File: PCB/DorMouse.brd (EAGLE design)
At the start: 63.3 x 90.1 mm, 55 parts, among them IC1 LM340MP-05, IC2 MAX1551, U1 STM32F10XRXT6, X1 MINI-USB-UX60-MB-5ST

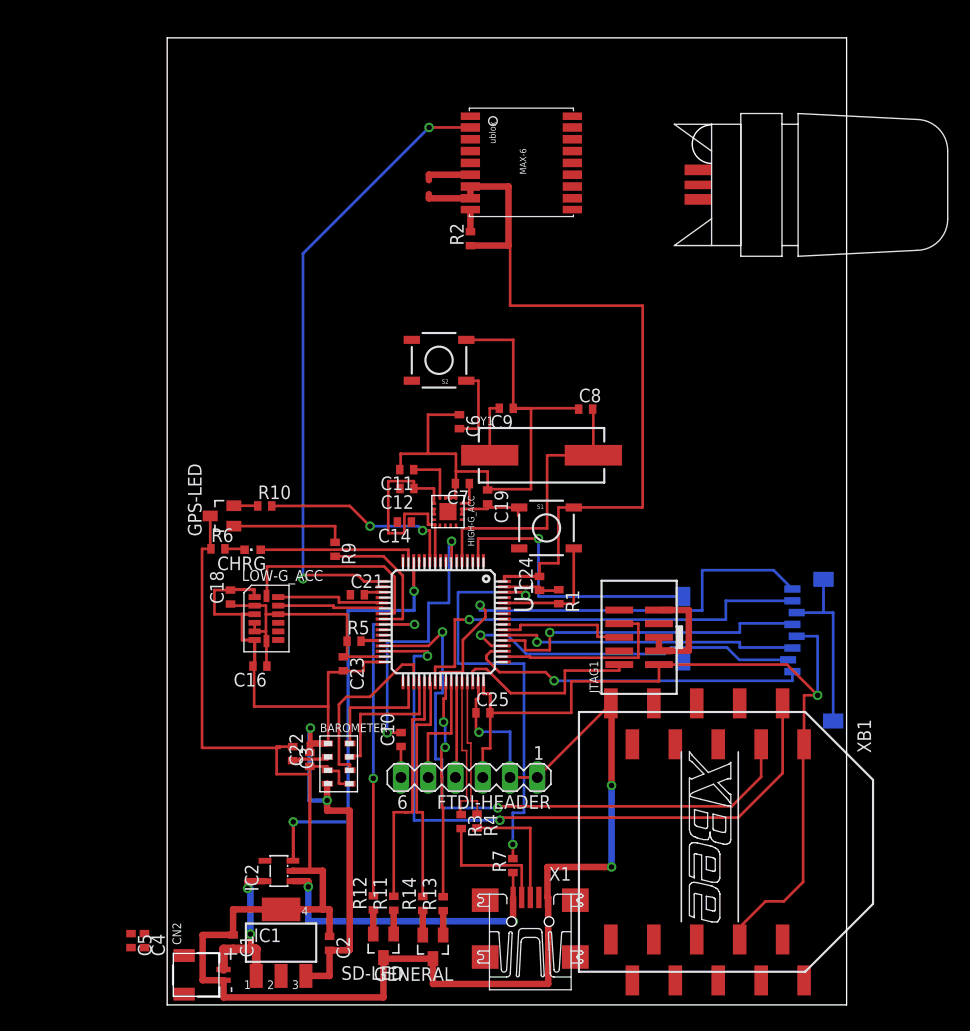
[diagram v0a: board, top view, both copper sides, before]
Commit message: Sync older board with schematic
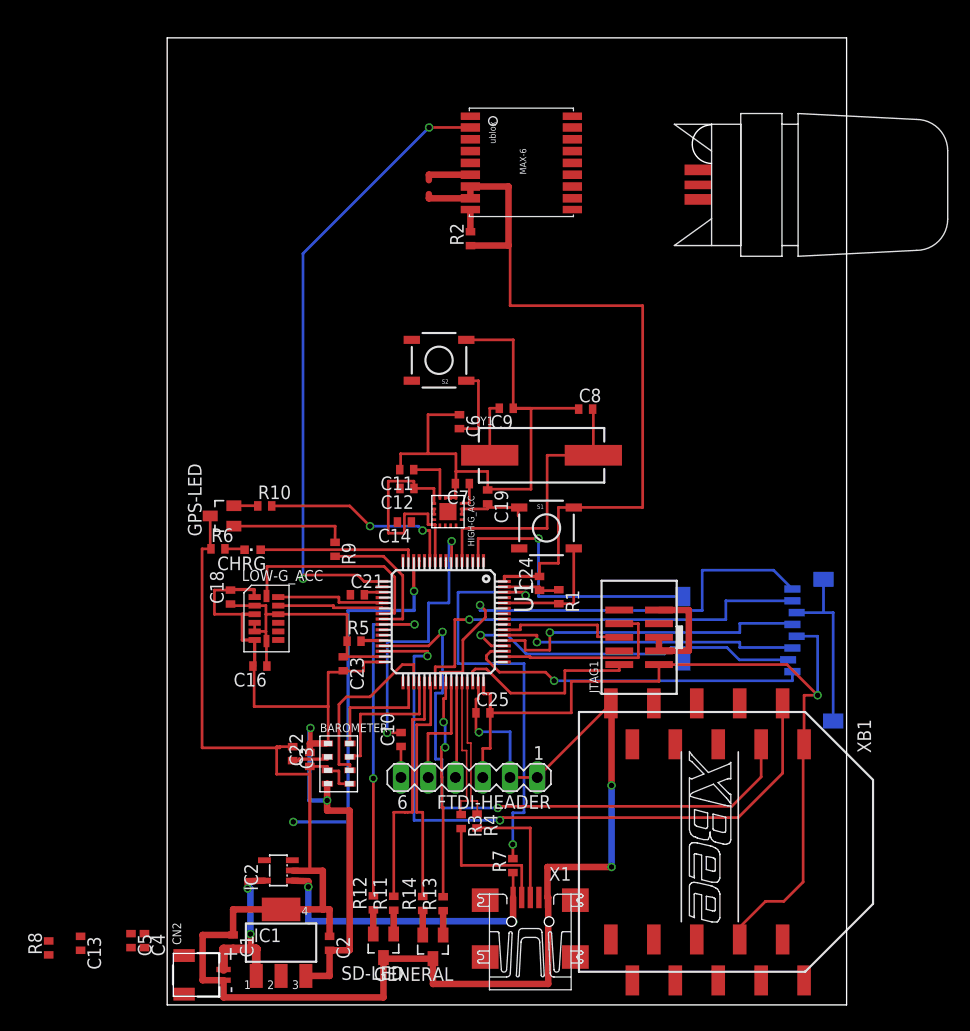
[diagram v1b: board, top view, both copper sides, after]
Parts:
- added C13: 1uF, rcl:C0402
- added R8: 100k, rcl:R0402
- moved IC2 0.07 mm to (10.4, 12.5)
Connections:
- new net N$13: IC2.3, R8.1
- net CHARGING(-): now also R8.2; no longer IC2.3
- net GND: now also C13.1
- net USB-5V: now also C13.2
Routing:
- net CHARGING(-): track 39.3 -> 35.6 mm
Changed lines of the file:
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@@
 </class>
 </classes>
-<designrules name="default">
+<designrules name="Fusion_eagle_rule_v1.1">
 <description language="de">&lt;b&gt;EAGLE Design Rules&lt;/b&gt;
 &lt;p&gt;
@@
 necessary adjustments and save your customized
 design rules under a new name.</description>
+<description language="zh">&lt;b&gt;Seeed Studio EAGLE Design Rules&lt;/b&gt;
+</description>
 <param name="layerSetup" value="(1*16)"/>
 <param name="mtCopper" value="0.035mm 0.035mm 0.035mm 0.035mm 0.035mm 0.035mm 0.035mm 0.035mm 0.035mm 0.035mm 0.035mm 0.035mm 0.035mm 0.035mm 0.035mm 0.035mm"/>
 <param name="mtIsolate" value="1.5mm 0.15mm 0.2mm 0.15mm 0.2mm 0.15mm 0.2mm 0.15mm 0.2mm 0.15mm 0.2mm 0.15mm 0.2mm 0.15mm 0.2mm"/>
-<param name="mdWireWire" value="8mil"/>
-<param name="mdWirePad" value="8mil"/>
-<param name="mdWireVia" value="8mil"/>
-<param name="mdPadPad" value="8mil"/>
-<param name="mdPadVia" value="8mil"/>
-<param name="mdViaVia" value="8mil"/>
-<param name="mdSmdPad" value="8mil"/>
-<param name="mdSmdVia" value="8mil"/>
-<param name="mdSmdSmd" value="8mil"/>
+<param name="mdWireWire" value="6mil"/>
+<param name="mdWirePad" value="6mil"/>
+<param name="mdWireVia" value="6mil"/>
+<param name="mdPadPad" value="6mil"/>
+<param name="mdPadVia" value="6mil"/>
+<param name="mdViaVia" value="6mil"/>
+<param name="mdSmdPad" value="0mil"/>
+<param name="mdSmdVia" value="0mil"/>
+<param name="mdSmdSmd" value="0mil"/>
 <param name="mdViaViaSameLayer" value="8mil"/>
 <param name="mnLayersViaInSmd" value="2"/>
-<param name="mdCopperDimension" value="40mil"/>
-<param name="mdDrill" value="8mil"/>
+<param name="mdCopperDimension" value="10mil"/>
+<param name="mdDrill" value="10mil"/>
 <param name="mdSmdStop" value="0mil"/>
-<param name="msWidth" value="10mil"/>
-<param name="msDrill" value="24mil"/>
-<param name="msMicroVia" value="9.99mm"/>
+<param name="msWidth" value="6mil"/>
+<param name="msDrill" value="12mil"/>
+<param name="msMicroVia" value="12mil"/>
 <param name="msBlindViaRatio" value="0.5"/>
 <param name="rvPadTop" value="0.25"/>
@@
 <param name="rlMinPadBottom" value="10mil"/>
 <param name="rlMaxPadBottom" value="20mil"/>
-<param name="rlMinViaOuter" value="8mil"/>
+<param name="rlMinViaOuter" value="6mil"/>
 <param name="rlMaxViaOuter" value="20mil"/>
-<param name="rlMinViaInner" value="8mil"/>
+<param name="rlMinViaInner" value="6mil"/>
 <param name="rlMaxViaInner" value="20mil"/>
 <param name="rlMinMicroViaOuter" value="4mil"/>
@@
 <param name="psTop" value="-1"/>
 <param name="psBottom" value="-1"/>
-<param name="psFirst" value="-1"/>
+<param name="psFirst" value="0"/>
 <param name="psElongationLong" value="100"/>
 <param name="psElongationOffset" value="100"/>
 <param name="mvStopFrame" value="1"/>
 <param name="mvCreamFrame" value="0"/>
-<param name="mlMinStopFrame" value="4mil"/>
-<param name="mlMaxStopFrame" value="4mil"/>
+<param name="mlMinStopFrame" value="2mil"/>
+<param name="mlMaxStopFrame" value="2mil"/>
 <param name="mlMinCreamFrame" value="0mil"/>
 <param name="mlMaxCreamFrame" value="0mil"/>
-<param name="mlViaStopLimit" value="0mil"/>
+<param name="mlViaStopLimit" value="100mil"/>
 <param name="srRoundness" value="0"/>
 <param name="srMinRoundness" value="0mil"/>
@@
 <param name="checkAngle" value="0"/>
 <param name="checkFont" value="1"/>
-<param name="checkRestrict" value="1"/>
+<param name="checkRestrict" value="0"/>
 <param name="useDiameter" value="13"/>
 <param name="maxErrors" value="50"/>
@@
 <element name="C1" library="rcl" package="C0402" value="0.22uF" x="6.14" y="5.87" rot="R270"/>
 <element name="C2" library="rcl" package="C0402" value="0.1uF" x="15.13" y="5.74" rot="R270"/>
-<element name="IC2" library="maxim" package="SOT23-5L" value="MAX1551" x="10.41" y="12.48" rot="R90">
-<attribute name="OC_NEWARK" value="88H0599" x="70.1" y="83.6" size="1.778" layer="27" rot="R90" display="off"/>
-<attribute name="MPN" value="MAX1551EZK-T" x="70.1" y="83.6" size="1.778" layer="27" rot="R90" display="off"/>
-<attribute name="MF" value="MAXIM" x="70.1" y="83.6" size="1.778" layer="27" rot="R90" display="off"/>
-<attribute name="OC_FARNELL" value="1628221" x="70.1" y="83.6" size="1.778" layer="27" rot="R90" display="off"/>
+<element name="IC2" library="maxim" package="SOT23-5L" value="MAX1551" x="10.36" y="12.53" rot="R90">
+<attribute name="OC_NEWARK" value="88H0599" x="70.05" y="83.65" size="1.778" layer="27" rot="R90" display="off"/>
+<attribute name="MPN" value="MAX1551EZK-T" x="70.05" y="83.65" size="1.778" layer="27" rot="R90" display="off"/>
+<attribute name="MF" value="MAXIM" x="70.05" y="83.65" size="1.778" layer="27" rot="R90" display="off"/>
+<attribute name="OC_FARNELL" value="1628221" x="70.05" y="83.65" size="1.778" layer="27" rot="R90" display="off"/>
 </element>
 <element name="X1" library="con-hirose" package="UX60-MB-5ST" value="MINI-USB-UX60-MB-5ST" x="33.83" y="7.76" rot="R90">
@@
 <element name="C5" library="rcl" package="C0402" value="4.7uF" x="-3.37" y="5.99" rot="R270"/>
 <element name="U$1" library="Ava" package="SARANTEL-SR1202" value="SARANTEL-SR1202" x="49.45" y="76.4"/>
+<element name="C13" library="rcl" package="C0402" value="1uF" x="-8.07" y="5.74" rot="R270"/>
+<element name="R8" library="rcl" package="R0402" value="100k" x="-11.04" y="5.31" rot="R90"/>
 </elements>
 <signals>
@@
 <wire x1="15.13" y1="8.899" x2="14.5" y2="8.899" width="0.6096" layer="1"/>
 <wire x1="14.5" y1="8.899" x2="10.61" y2="8.899" width="0.6096" layer="1"/>
-<wire x1="11.71" y1="12.48" x2="11.71" y2="12.5" width="0.6096" layer="1"/>
+<wire x1="11.66" y1="12.53" x2="11.71" y2="12.5" width="0" layer="19" extent="1-16"/>
 <wire x1="11.71" y1="12.5" x2="14.5" y2="12.5" width="0.6096" layer="1"/>
 <wire x1="14.5" y1="12.5" x2="14.5" y2="8.899" width="0.6096" layer="1"/>
@@
 <contactref element="U1" pad="12"/>
 <wire x1="23.97" y1="41.4" x2="24" y2="41.4" width="0.254" layer="1"/>
+<contactref element="C13" pad="1"/>
 <wire x1="49.45" y1="75.05" x2="49.45" y2="77.8" width="0" layer="19" extent="1-1"/>
 <wire x1="37.75" y1="74.1" x2="49.45" y2="75.05" width="0" layer="19" extent="1-1"/>
@@
 <wire x1="-2.12" y1="5.34" x2="3.3" y2="6.52" width="0" layer="19" extent="1-1"/>
 <wire x1="-3.37" y1="6.64" x2="-2.12" y2="5.34" width="0" layer="19" extent="1-1"/>
+<wire x1="-8.07" y1="6.39" x2="-3.37" y2="6.64" width="0" layer="19" extent="1-1"/>
 <wire x1="45.82" y1="33" x2="41.4" y2="28.098" width="0" layer="19" extent="1-1"/>
 <wire x1="48.05" y1="32.05" x2="48.6" y2="33" width="0" layer="19" extent="1-16"/>
@@
 <wire x1="8.2986" y1="5.22" x2="8.2986" y2="5.2" width="0.8128" layer="1"/>
 <wire x1="8.2986" y1="5.2" x2="7.4" y2="5.2" width="0.8128" layer="1"/>
-<wire x1="9.11" y1="11.53" x2="7.5" y2="11.53" width="0.6096" layer="1"/>
+<wire x1="9.06" y1="11.58" x2="7.5" y2="11.53" width="0.6096" layer="1"/>
 <wire x1="7.5" y1="11.53" x2="7.5" y2="10.85" width="0.6096" layer="1"/>
 <via x="7.5" y="10.85" extent="1-16" drill="0.5" shape="octagon"/>
@@
 <contactref element="X1" pad="1"/>
 <contactref element="R7" pad="1"/>
-<wire x1="11.71" y1="11.53" x2="13.15" y2="11.53" width="0.6096" layer="1"/>
+<wire x1="11.66" y1="11.58" x2="13.15" y2="11.53" width="0.6096" layer="1"/>
 <wire x1="13.15" y1="11.53" x2="13.15" y2="11" width="0.6096" layer="1"/>
 <via x="13.15" y="11" extent="1-16" drill="0.5" shape="octagon"/>
@@
 <wire x1="32.23" y1="10.01" x2="32.23" y2="12.33" width="0.254" layer="1"/>
 <wire x1="32.23" y1="12.33" x2="32.21" y2="12.33" width="0.254" layer="1"/>
+<contactref element="C13" pad="2"/>
+<wire x1="-8.07" y1="5.09" x2="11.66" y2="11.58" width="0" layer="19" extent="1-1"/>
 </signal>
 <signal name="CHARGING(-)">
-<contactref element="IC2" pad="3"/>
 <contactref element="U1" pad="14"/>
-<wire x1="11.71" y1="13.43" x2="11.75" y2="13.43" width="0.3048" layer="1"/>
-<wire x1="11.75" y1="13.43" x2="11.75" y2="17.05" width="0.3048" layer="1"/>
 <via x="11.75" y="17.05" extent="1-16" drill="0.5" shape="octagon"/>
 <wire x1="11.75" y1="17.05" x2="16.85" y2="17.05" width="0.3048" layer="16"/>
@@
 <wire x1="23" y1="38.55" x2="22.97" y2="38.55" width="0.3048" layer="1"/>
 <wire x1="22.97" y1="38.55" x2="22.97" y2="41.4" width="0.3048" layer="1"/>
+<contactref element="R8" pad="2"/>
+<wire x1="-11.04" y1="5.96" x2="22.97" y2="41.4" width="0" layer="19" extent="1-16"/>
 </signal>
 <signal name="MOSI-1">
@@
 <wire x1="33.4" y1="38.45" x2="31.42" y2="38.45" width="0.254" layer="1"/>
 </signal>
+<signal name="N$13">
+<contactref element="R8" pad="1"/>
+<contactref element="IC2" pad="3"/>
+<wire x1="11.66" y1="13.48" x2="-11.04" y2="4.66" width="0" layer="19" extent="1-16"/>
+</signal>
 </signals>

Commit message: Most of the pcb done
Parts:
- removed C4: 10nF, rcl:C0402
- moved C5 42.5 mm to (15.0, 44.3), turned to 180 degrees
- moved C18 28.1 mm to (22.2, 60.9), turned to 270 degrees
- moved R8 26.4 mm to (11.3, 19.4), turned to 180 degrees
- moved XB1 24.0 mm to (26.7, 11.1), flipped to the bottom, turned to 180 degrees
- moved U$1 21.4 mm to (36.6, 59.3)
- moved CN1 18.8 mm to (28.8, 41.1)
- moved S2 18.6 mm to (8.62, 51.8), turned to 0 degrees
- moved C13 18.2 mm to (6.92, 16.0), turned to 90 degrees
- moved GPS 16.3 mm to (29.3, 62.6)
- moved R2 14.4 mm to (21.0, 59.0), turned to 270 degrees
- moved C6 14.3 mm to (12.9, 53.4)
- moved X1 11.2 mm to (22.6, 7.78), turned to 180 degrees
- moved R11 9.82 mm to (19.6, 19.2)
- moved R12 9.82 mm to (17.7, 19.2)
- moved SD-LED 9.82 mm to (18.6, 15.2)
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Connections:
- net GND: no longer C4.2
- net VCC: no longer C4.1
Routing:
- net GND: track 294.8 -> 379.9 mm, vias 3 -> 8
- net RESET: track 34.7 -> 82.2 mm, vias 2 -> 4
- net U2-TX: track 0.00 -> 42.0 mm, vias 0 -> 2
- net TIMEPULSE: track 0.00 -> 39.3 mm, vias 0 -> 2
- net USB-5V: track 29.0 -> 62.9 mm, vias 2 -> 0
- net U3-TX: track 57.8 -> 41.3 mm, vias 2 -> 1
- net U3-RX: track 63.9 -> 48.0 mm, vias 2 -> 1
- net N$6: track 5.27 -> 18.9 mm, vias 0 -> 2
- net TCK: track 0.00 -> 13.5 mm, vias 0 -> 2
- net VCC: track 247.8 -> 235.9 mm, vias 3 -> 6
- net SD-CLK: track 30.3 -> 19.0 mm
- net SD-DAT0: track 40.9 -> 30.0 mm
- net SD-DAT1: track 44.5 -> 33.5 mm
- net SD-DET: track 26.5 -> 15.6 mm
- net SD-DAT2: track 32.4 -> 21.5 mm
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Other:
- board size 63.3 x 90.1 mm -> 44.9 x 68.5 mm

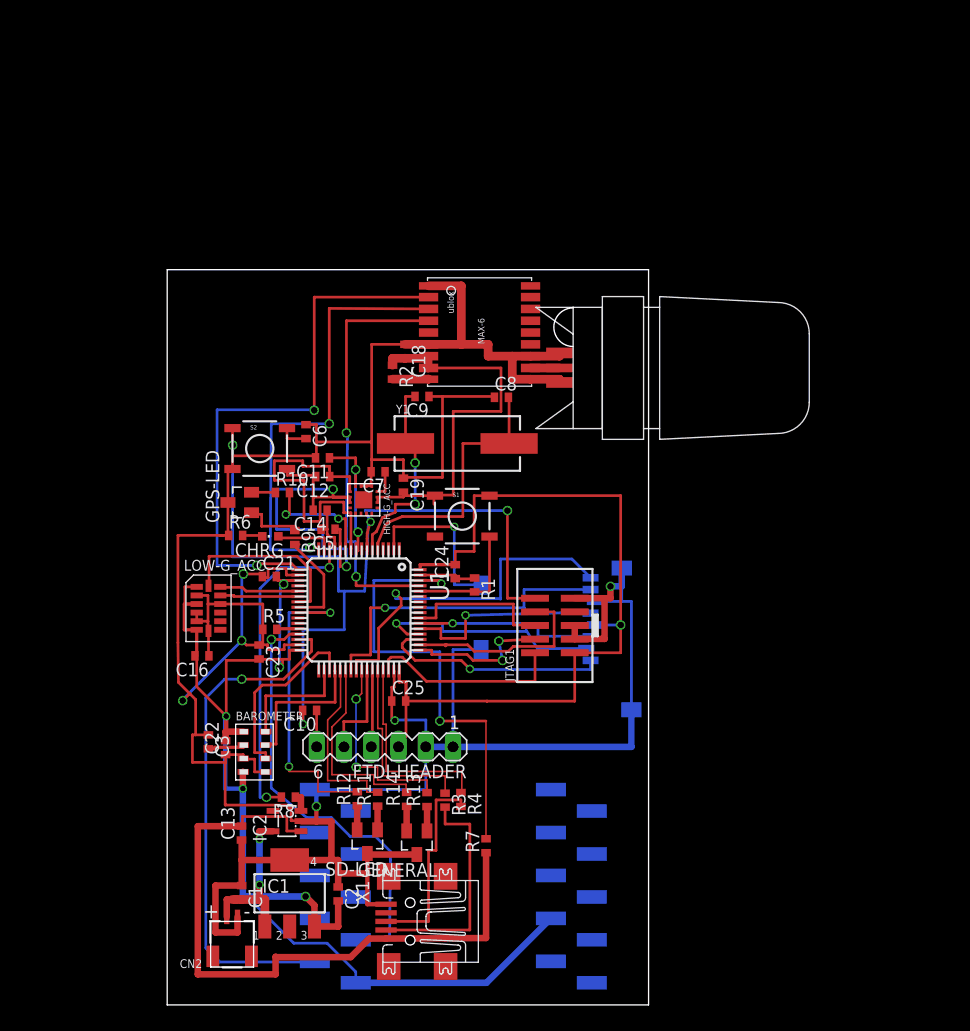
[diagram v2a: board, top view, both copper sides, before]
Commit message: PCB r1 - Finished
Al wires routed
No overlaps
Total size - 41x70mm
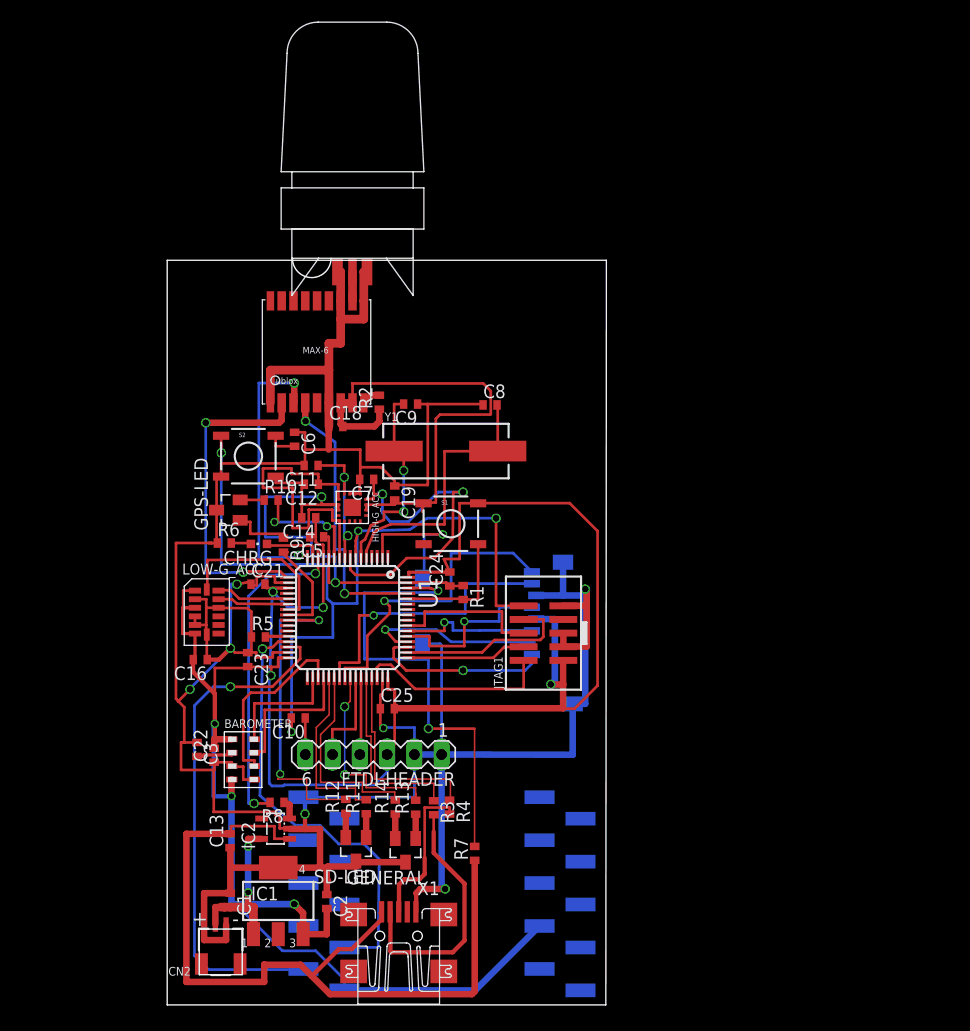
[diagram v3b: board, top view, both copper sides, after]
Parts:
- moved U$1 21.3 mm to (17.3, 68.3), turned to 90 degrees
- moved GPS 15.4 mm to (14.0, 61.0), turned to 270 degrees
- moved C18 9.51 mm to (15.7, 53.9), turned to 0 degrees
- moved CN1 5.50 mm to (23.3, 41.6)
- moved R2 3.06 mm to (19.8, 56.2), turned to 90 degrees
- moved X1 1.73 mm to (21.6, 6.42), turned to 90 degrees
- moved C8 1.28 mm to (30.1, 55.9)
- moved FTDI-HEADER 1.28 mm to (19.2, 23.3)
- moved R1 1.28 mm to (27.6, 38.4)
- moved R12 1.28 mm to (16.6, 18.5)
- moved R4 1.28 mm to (26.3, 18.4)
- moved R7 1.28 mm to (28.6, 14.1)
- moved Y1 1.28 mm to (26.0, 51.6)
- moved GENERAL 1.28 mm to (22.2, 14.4)
- moved BAROMETER 1.28 mm to (5.67, 20.8)
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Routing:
- net VCC: track 235.9 -> 307.3 mm, vias 6 -> 7
- net ADC1: track 2.58 -> 31.9 mm, vias 0 -> 2
- net U2-RX: track 52.6 -> 30.6 mm
- net U2-TX: track 42.0 -> 26.2 mm
- net USB-5V: track 62.9 -> 76.7 mm
- net TIMEPULSE: track 39.3 -> 26.1 mm
- net SD-DAT3: track 22.1 -> 16.4 mm
- net SD-DAT2: track 21.5 -> 16.8 mm
- net USB-DP: track 18.9 -> 14.5 mm
- net SD-DAT1: track 33.5 -> 29.3 mm
- net SD-CMD: track 17.1 -> 13.1 mm
- net SD-DAT0: track 30.0 -> 26.8 mm
- net SD-CLK: track 19.0 -> 16.1 mm
- net GND: track 379.9 -> 382.7 mm, vias 8 -> 9
- net USB-DM: track 21.6 -> 24.0 mm
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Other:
- board size 44.9 x 68.5 mm -> 40.9 x 69.4 mm
